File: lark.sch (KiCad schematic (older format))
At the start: 41 parts, among them J1 SPI, J2 UART0, J3 I2C_0, SW1 SW_ENTR, SW2 SW_UP, SW3 SW_DOWN, SW4 SW_VARIO

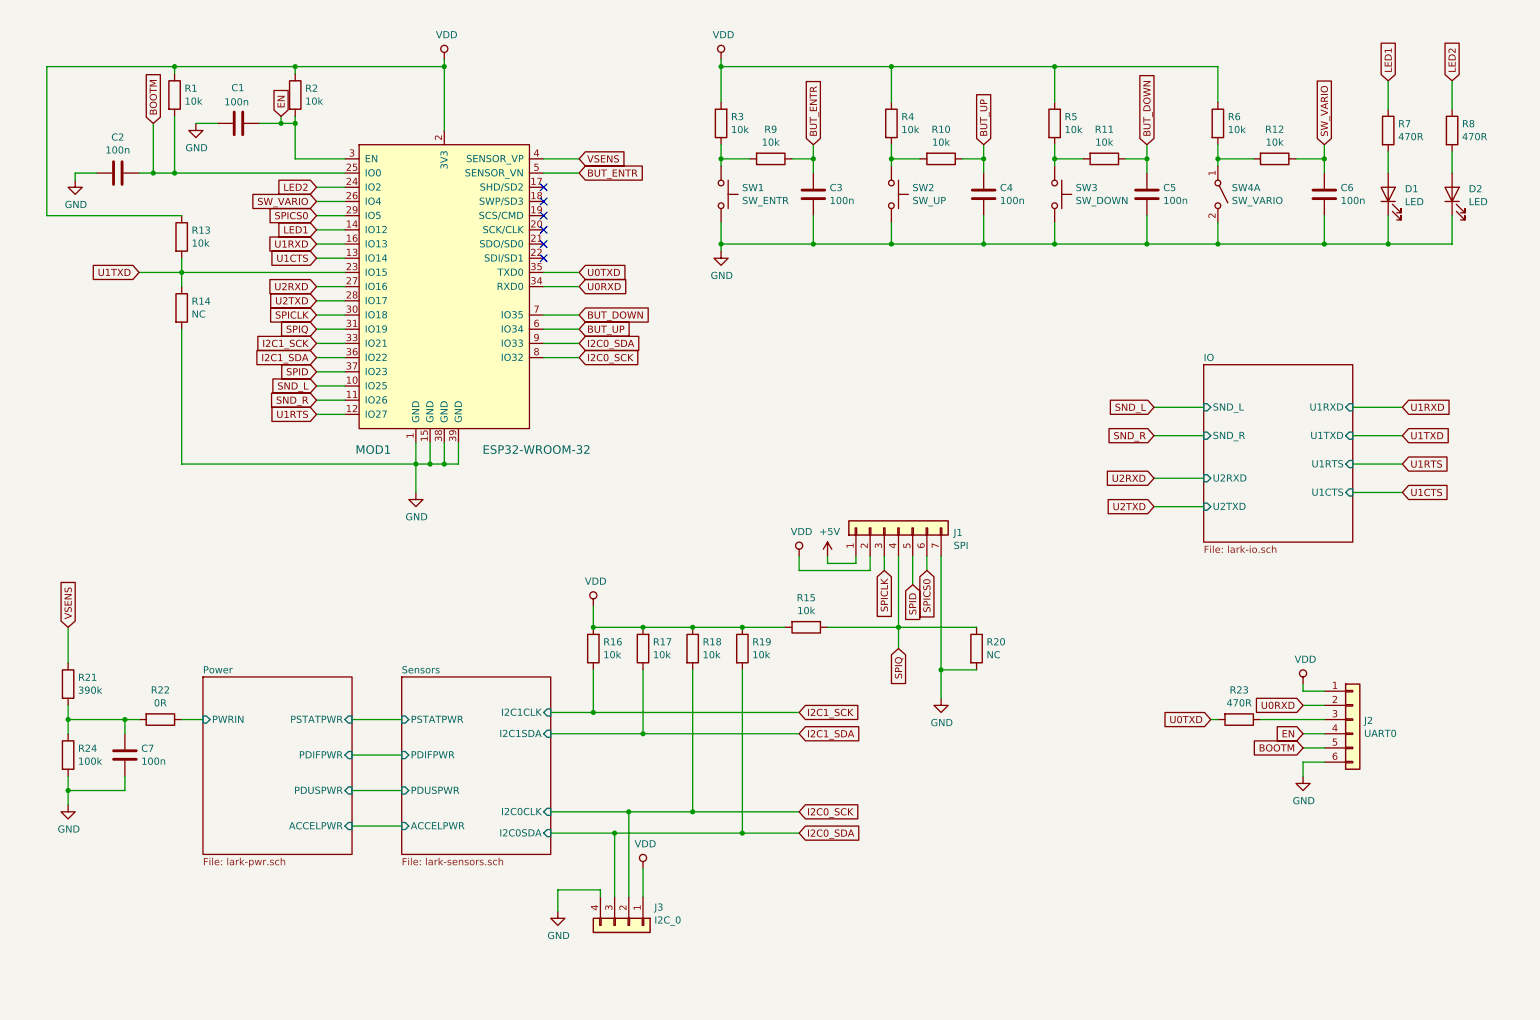
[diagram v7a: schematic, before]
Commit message: Updating schematic for the first prototype
* U1 can supply up to 600 mA
* drop USB charger for now
* smaller type of DC/DC (U2) for input
* remove one of the large capacitors
* change BMX interface to 4-wire SPI for speed reasons
* add I2C mux for pressure sensors

The changes were made during the meeting with Tomas.

BMX055 will be replaced by BMX088. For mechanical reasons, the pressure
sensors will be placed on a daughterboard. The daughterboard could get
footprints for different kinds pressure sensors (i.e. BMP388, HCLA0025).
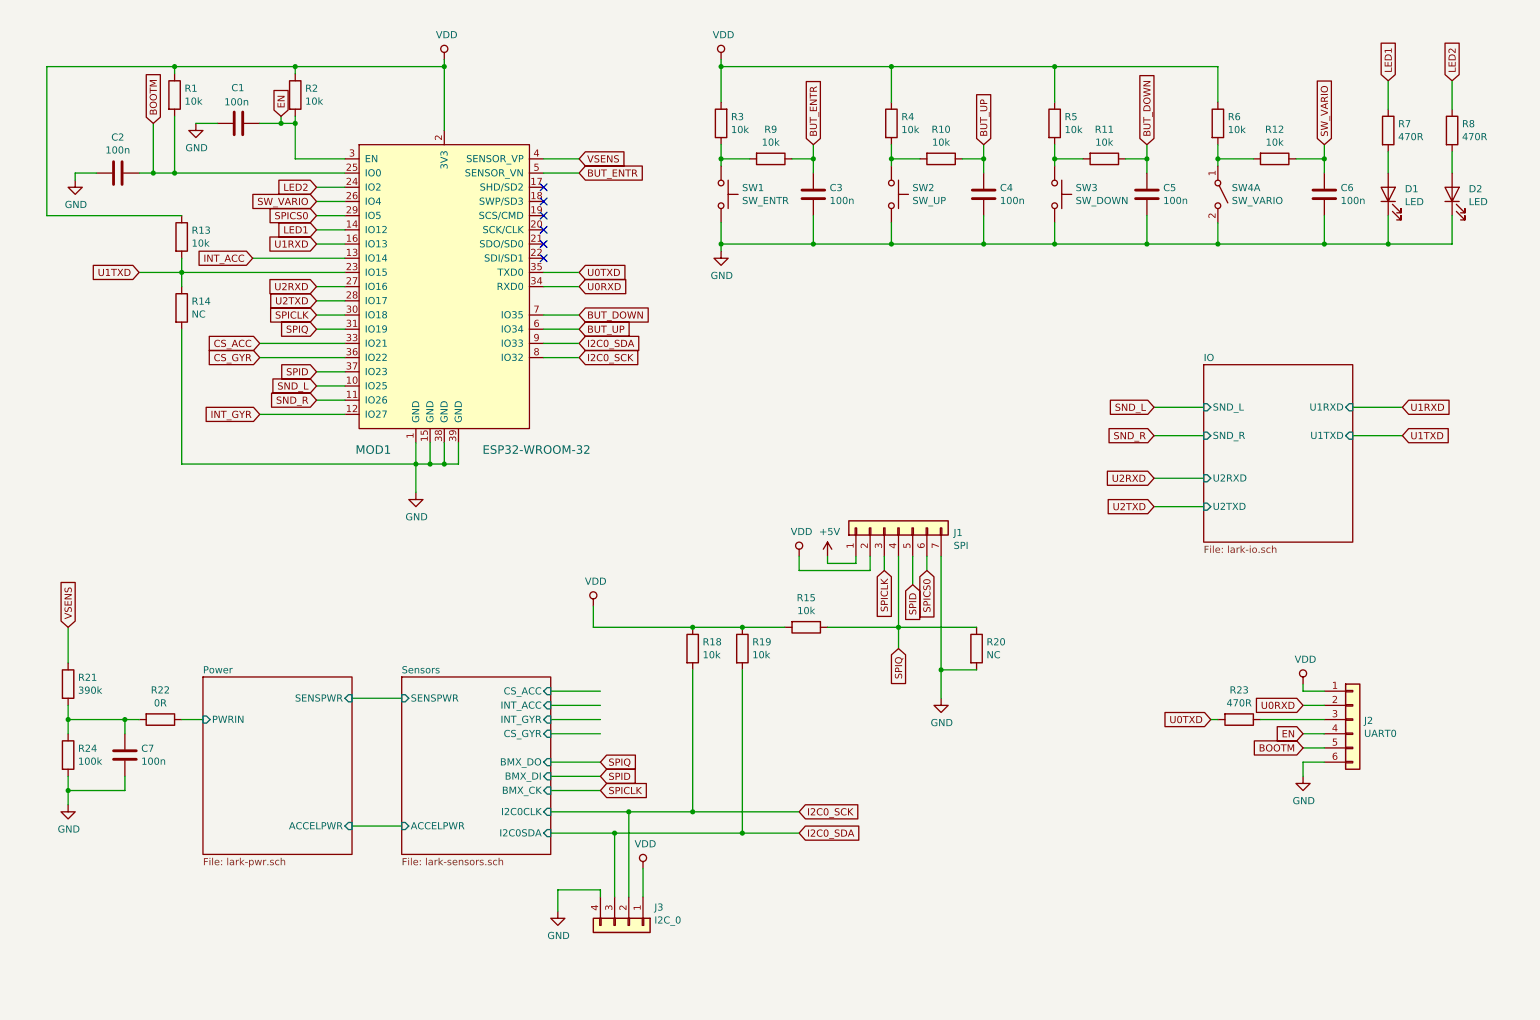
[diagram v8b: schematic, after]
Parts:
- removed R16, R17: 10k, Resistor_SMD:R_0805_2012Metric_Pad1.15x1.40mm_HandSolder, symbol lark-rescue:R-Device
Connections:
- net I2C1_SCK renamed CS_ACC
- net I2C1_SDA renamed CS_GYR
- net U1CTS renamed INT_ACC
- net U1RTS renamed INT_GYR
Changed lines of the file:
@@
 F1 "lark-pwr.sch" 50
 F2 "PWRIN" I L 1850 5600 50
-F3 "PSTATPWR" I R 2900 5600 50
-F4 "ACCELPWR" I R 2900 6350 50
-F5 "PDIFPWR" I R 2900 5850 50
-F6 "PDUSPWR" I R 2900 6100 50
+F3 "ACCELPWR" I R 2900 6350 50
+F4 "SENSPWR" I R 2900 5450 50
 $EndSheet
 $Comp
@@
 F0 "Sensors" 50
 F1 "lark-sensors.sch" 50
-F2 "PSTATPWR" I L 3250 5600 50
-F3 "PDUSPWR" I L 3250 6100 50
-F4 "PDIFPWR" I L 3250 5850 50
-F5 "ACCELPWR" I L 3250 6350 50
-F6 "I2C0CLK" I R 4300 6250 50
-F7 "I2C0SDA" I R 4300 6400 50
-F8 "I2C1SDA" I R 4300 5700 50
-F9 "I2C1CLK" I R 4300 5550 50
+F2 "ACCELPWR" I L 3250 6350 50
+F3 "I2C0CLK" I R 4300 6250 50
+F4 "I2C0SDA" I R 4300 6400 50
+F5 "SENSPWR" I L 3250 5450 50
+F6 "CS_ACC" I R 4300 5400 50
+F7 "CS_GYR" I R 4300 5700 50
+F8 "BMX_DO" I R 4300 5900 50
+F9 "BMX_DI" I R 4300 6000 50
+F10 "BMX_CK" I R 4300 6100 50
+F11 "INT_ACC" I R 4300 5500 50
+F12 "INT_GYR" I R 4300 5600 50
 $EndSheet
 Text GLabel 4500 1650 2    50   Input ~ 0
@@
 Text GLabel 2650 3350 0    50   Input ~ 0
 SND_R
-Text GLabel 2650 3450 0    50   Input ~ 0
-U1RTS
-Text GLabel 2650 2350 0    50   Input ~ 0
-U1CTS
 Text GLabel 2650 2150 0    50   Input ~ 0
 LED1
@@
 	2650 2250 2850 2250
 Wire Wire Line
-	2650 2350 2850 2350
-Wire Wire Line
 	2650 3150 2850 3150
 Wire Wire Line
@@
 Wire Wire Line
 	2650 3350 2850 3350
-Wire Wire Line
-	2850 3450 2650 3450
 Wire Wire Line
 	2650 2150 2850 2150
@@
 Wire Wire Line
 	2850 2850 2650 2850
-Text GLabel 2650 2950 0    50   Input ~ 0
-I2C1_SCK
-Wire Wire Line
-	2650 2950 2850 2950
 Text GLabel 4500 2550 2    50   Input ~ 0
 U0RXD
@@
 Wire Wire Line
 	4500 3050 4250 3050
-Text GLabel 2650 3050 0    50   Input ~ 0
-I2C1_SDA
-Wire Wire Line
-	2850 3050 2650 3050
-Text GLabel 6050 5550 2    50   Input ~ 0
-I2C1_SCK
-Text GLabel 6050 5700 2    50   Input ~ 0
-I2C1_SDA
-$Comp
-L lark-rescue:R-Device R16
-U 1 1 5C5EB518
-P 4600 5100
-F 0 "R16" H 4530 5054 50  0000 R CNN
-F 1 "10k" H 4530 5145 50  0000 R CNN
-F 2 "Resistor_SMD:R_0805_2012Metric_Pad1.15x1.40mm_HandSolder" V 4530 5100 50  0001 C CNN
-F 3 "~" H 4600 5100 50  0001 C CNN
-F 4 "RC0805FR-0710KL" H 4600 5100 50  0001 C CNN "MPN"
-	1    4600 5100
-	-1   0    0    1
-$EndComp
-$Comp
-L lark-rescue:R-Device R17
-U 1 1 5C5EB606
-P 4950 5100
-F 0 "R17" H 4880 5054 50  0000 R CNN
-F 1 "10k" H 4880 5145 50  0000 R CNN
-F 2 "Resistor_SMD:R_0805_2012Metric_Pad1.15x1.40mm_HandSolder" V 4880 5100 50  0001 C CNN
-F 3 "~" H 4950 5100 50  0001 C CNN
-F 4 "RC0805FR-0710KL" H 4950 5100 50  0001 C CNN "MPN"
-	1    4950 5100
-	-1   0    0    1
-$EndComp
 $Comp
 L lark-rescue:VDD-power #PWR09
@@
 Wire Wire Line
 	4600 4800 4600 4950
-Wire Wire Line
-	4600 4950 4950 4950
-Connection ~ 4600 4950
-Wire Wire Line
-	4950 4950 5300 4950
-Connection ~ 4950 4950
 Text GLabel 6050 6250 2    50   Input ~ 0
 I2C0_SCK
@@
 	5650 4950 5950 4950
 Connection ~ 5650 4950
-Wire Wire Line
-	2900 5600 3250 5600
-Wire Wire Line
-	2900 5850 3250 5850
-Wire Wire Line
-	3250 6100 2900 6100
 Wire Wire Line
 	2900 6350 3250 6350
@@
 F4 "U1RXD" I R 9950 3400 50
 F5 "U1TXD" I R 9950 3600 50
-F6 "U1RTS" I R 9950 3800 50
-F7 "U1CTS" I R 9950 4000 50
-F8 "U2RXD" I L 8900 3900 50
-F9 "U2TXD" I L 8900 4100 50
+F6 "U2RXD" I L 8900 3900 50
+F7 "U2TXD" I L 8900 4100 50
 $EndSheet
 $Comp
@@
 Text GLabel 10300 3600 2    50   Input ~ 0
 U1TXD
-Text GLabel 10300 3800 2    50   Input ~ 0
-U1RTS
-Text GLabel 10300 4000 2    50   Input ~ 0
-U1CTS
 Wire Wire Line
 	10300 3400 9950 3400
@@
 	9950 3600 10300 3600
 Wire Wire Line
-	10300 3800 9950 3800
-Wire Wire Line
-	9950 4000 10300 4000
-Wire Wire Line
 	8900 4100 8550 4100
 Wire Wire Line
@@
 Wire Wire Line
 	4300 6400 4750 6400
-Wire Wire Line
-	6050 5550 4600 5550
-Wire Wire Line
-	6050 5700 4950 5700
-Wire Wire Line
-	4600 5250 4600 5550
-Connection ~ 4600 5550
-Wire Wire Line
-	4600 5550 4300 5550
-Wire Wire Line
-	4950 5250 4950 5700
-Connection ~ 4950 5700
-Wire Wire Line
-	4950 5700 4300 5700
 Wire Wire Line
 	5300 5250 5300 6250
@@
 Wire Wire Line
 	4350 6800 4350 6950
+Wire Wire Line
+	4600 4950 5300 4950
+Wire Wire Line
+	2900 5450 3250 5450
+Wire Wire Line
+	4300 6000 4650 6000
+Wire Wire Line
+	4300 6100 4650 6100
+Wire Wire Line
+	4300 5900 4650 5900
+Text GLabel 4650 6000 2    50   Input ~ 0
+SPID
+Text GLabel 4650 5900 2    50   Input ~ 0
+SPIQ
+Text GLabel 4650 6100 2    50   Input ~ 0
+SPICLK
+Wire Wire Line
+	4300 5700 4650 5700
+Wire Wire Line
+	4300 5400 4650 5400
+Wire Wire Line
+	4300 5500 4650 5500
+Wire Wire Line
+	4300 5600 4650 5600
+Wire Wire Line
+	2850 2950 2250 2950
+Wire Wire Line
+	2850 3050 2250 3050
+Text GLabel 2250 2950 0    50   Input ~ 0
+CS_ACC
+Text GLabel 2250 3050 0    50   Input ~ 0
+CS_GYR
+Wire Wire Line
+	2200 2350 2850 2350
+Wire Wire Line
+	2250 3450 2850 3450
+Text GLabel 2250 3450 0    50   Input ~ 0
+INT_GYR
+Text GLabel 2200 2350 0    50   Input ~ 0
+INT_ACC
 $EndSCHEMATC
